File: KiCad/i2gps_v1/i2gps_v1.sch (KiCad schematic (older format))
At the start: 58 parts, among them IC1 ATMEGA8-AI, P1 I/O, P10 CD2, P11 CD2, P12 CD1, P13 CD1, P2 COMM_R, P3 BootDrive, P4 CONN_6, P5 CONN_6, P6 CONN_2, P7 GPS_UP501, P8 FTDI, P9 ISP, SW1 SW_PUSH, U1 MCP1700T-3302E/TT, U2 74HC125, U3 MIC5219-5.0BM5, X1 CRYSTAL_2

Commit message: i2gps_v1 : some minor mods. uploading so I can go home and work on it.
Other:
- note added: "B14 (PD5)\nBootDrive Header"
- note added: "B_03 (PD2)\nGPS 1pps"
- note added: "B_12 (PD7)\nSQW (1pps) signal"
- note removed: "B14 (PD5) : for\nBootDrive Header"
- note removed: "B_03 : GPS 1pps"
- note removed: "SQW signal\ncomes to PD7 / B12"
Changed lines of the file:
@@
-EESchema Schematic File Version 2  date 2/23/2012 11:50:56 AM
+EESchema Schematic File Version 2  date 2/23/2012 5:46:03 PM
 LIBS:i2gps_v1
 LIBS:power
@@
 Comment4 ""
 $EndDescr
-Text Notes 7050 6300 0    60   Italic 12
-GPS Breakout
+Wire Notes Line
+	4050 3925 4050 3775
+Wire Notes Line
+	4050 3925 4750 3925
+Wire Notes Line
+	4750 3925 4750 3775
+Wire Notes Line
+	4750 3775 4050 3775
 Wire Notes Line
 	7050 7025 7050 6300
@@
 Connection ~ 10600 1850
 Wire Notes Line
-	4750 3675 4050 3675
-Wire Notes Line
-	4750 3675 4750 3525
-Wire Notes Line
-	4750 3525 4050 3525
-Wire Notes Line
-	4050 3525 4050 3675
+	4750 3750 4050 3750
+Wire Notes Line
+	4750 3750 4750 3600
+Wire Notes Line
+	4750 3600 4050 3600
+Wire Notes Line
+	4050 3600 4050 3750
 Wire Wire Line
 	4000 6900 3625 6900
@@
 Connection ~ 5000 2650
 Wire Wire Line
-	4800 1700 4800 4775
+	4800 1775 4800 4850
 Connection ~ 4800 2750
 Wire Wire Line
@@
 	10850 6700 10950 6700
 Wire Notes Line
-	4750 3750 4050 3750
-Wire Notes Line
-	4750 3750 4750 3950
-Wire Notes Line
-	4750 3950 4050 3950
-Wire Notes Line
-	4050 3950 4050 3750
-Wire Notes Line
 	3550 6300 4525 6300
 Wire Notes Line
@@
 	7675 6800 7275 6800
 Wire Notes Line
-	4750 3275 4050 3275
-Wire Notes Line
-	4750 3275 4750 3375
-Wire Notes Line
-	4750 3375 4050 3375
-Wire Notes Line
-	4050 3375 4050 3275
-Text Notes 4100 3350 0    40   Italic 8
-B_03 : GPS 1pps
+	4750 3425 4050 3425
+Wire Notes Line
+	4750 3425 4750 3575
+Wire Notes Line
+	4750 3575 4050 3575
+Wire Notes Line
+	4050 3575 4050 3425
+Text Notes 7050 6300 0    60   Italic 12
+GPS Breakout
+Text Notes 4100 3500 0    40   Italic 8
+B_03 (PD2)\nGPS 1pps
 Text Label 7275 6900 0    50   ~ 0
 B_03
@@
 Text Label 3625 6800 0    50   ~ 0
 B_14
-Text Notes 4100 3600 0    40   Italic 8
-B14 (PD5) : for\nBootDrive Header
+Text Notes 4100 3675 0    40   Italic 8
+B14 (PD5)\nBootDrive Header
 Text Label 3625 6900 0    50   ~ 0
 RXD
@@
 3V3
 Text Notes 4075 3850 0    40   Italic 8
-SQW signal\ncomes to PD7 / B12
+B_12 (PD7)\nSQW (1pps) signal
 Text Label 10950 6900 0    60   ~ 0
 BAT

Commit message: i2gps_v1 : this project is merged with i2sd_v3. GPS header to be added
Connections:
- net labels removed: B_12
- wire segments 236 -> 235
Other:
- note added: "B_12 (PD7)\nSQW (1Hz) signal"
- note removed: "B_12 (PD7)\nSQW (1pps) signal"
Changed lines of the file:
@@
-EESchema Schematic File Version 2  date 2/23/2012 5:46:03 PM
+EESchema Schematic File Version 2  date 3/9/2012 6:29:21 PM
 LIBS:i2gps_v1
 LIBS:power
@@
 Sheet 1 2
 Title "Buckler, i2sd, v3, with RTC, with HW addressing"
-Date "23 feb 2012"
+Date "9 mar 2012"
 Rev "3"
 Comp "WyoLum"
@@
 Comment4 ""
 $EndDescr
+Wire Wire Line
+	3400 2750 4800 2750
 Wire Notes Line
 	4050 3925 4050 3775
@@
 Connection ~ 6300 6700
 Wire Wire Line
-	6300 6700 6300 6800
+	6300 6800 6300 6700
 Wire Wire Line
 	6300 6800 6400 6800
@@
 	2900 7000 2000 7000
 Wire Wire Line
-	2700 7300 2700 7200
+	2700 7200 2700 7300
 Connection ~ 10600 2400
 Wire Wire Line
-	10850 2575 10850 2400
+	10850 2400 10850 2575
 Wire Wire Line
 	10850 2575 10700 2575
@@
 	10650 1350 10650 1450
 Wire Wire Line
-	10925 1350 10925 1450
+	10925 1450 10925 1350
 Wire Wire Line
 	10925 1450 8875 1450
@@
 	10400 850  10325 850
 Wire Wire Line
-	10325 1000 10450 1000
+	10450 1000 10325 1000
 Wire Wire Line
 	10450 1000 10450 700
@@
 Connection ~ 5750 1900
 Wire Wire Line
-	5750 1900 6150 1900
+	6150 1900 5750 1900
 Wire Wire Line
 	6150 1900 6150 1950
 Connection ~ 6300 2450
 Wire Wire Line
-	6150 2450 7100 2450
+	7100 2450 6150 2450
 Wire Wire Line
 	6150 2450 6150 2250
@@
 Connection ~ 5750 3100
 Wire Wire Line
-	6150 3100 5750 3100
+	5750 3100 6150 3100
 Connection ~ 6450 4050
 Wire Wire Line
@@
 	5750 1100 5750 4050
 Wire Wire Line
-	5750 4050 7000 4050
+	7000 4050 5750 4050
 Wire Wire Line
 	7000 4050 7000 4650
@@
 	4800 800  4800 1200
 Wire Wire Line
-	3400 2750 4800 2750
-Wire Wire Line
 	3400 2650 5000 2650
 Wire Wire Line
@@
 	5400 1200 5400 1100
 Wire Wire Line
-	5200 1200 5200 1100
+	5200 1100 5200 1200
 Connection ~ 7600 1100
 Connection ~ 1075 4975
@@
 	1500 2650 975  2650
 Wire Wire Line
-	975  2650 975  800
-Wire Wire Line
-	3400 4350 5400 4350
-Wire Wire Line
-	3400 4250 5200 4250
+	975  800  975  2650
+Wire Wire Line
+	5400 4350 3400 4350
+Wire Wire Line
+	5200 4250 3400 4250
 Connection ~ 8400 2400
 Connection ~ 8025 4975
@@
 	8025 4750 8425 4750
 Wire Wire Line
-	7950 4875 5000 4875
+	5000 4875 7950 4875
 Wire Wire Line
 	2350 800  2350 1950
@@
 	9950 2475 9950 2350
 Wire Wire Line
-	5200 4250 5200 1700
-Wire Wire Line
-	5400 4350 5400 1700
-Wire Wire Line
-	5000 4875 5000 1700
+	5200 1700 5200 4250
+Wire Wire Line
+	5400 1700 5400 4350
+Wire Wire Line
+	5000 1700 5000 4875
 Connection ~ 5000 2650
 Wire Wire Line
-	4800 1775 4800 4850
+	4800 1700 4800 4775
 Connection ~ 4800 2750
 Wire Wire Line
@@
 Connection ~ 7100 4975
 Wire Wire Line
-	7100 2450 7100 4975
+	7100 4975 7100 2450
 Connection ~ 7100 3650
 Wire Wire Line
@@
 	1150 6800 800  6800
 Wire Wire Line
-	6150 3450 6150 3650
-Wire Wire Line
-	6150 3650 7100 3650
+	6150 3650 6150 3450
+Wire Wire Line
+	7100 3650 6150 3650
 Connection ~ 6300 3650
 Wire Wire Line
-	6150 2850 6150 3050
-Wire Wire Line
-	6150 3050 7100 3050
+	6150 3050 6150 2850
+Wire Wire Line
+	7100 3050 6150 3050
 Connection ~ 6300 3050
 Wire Wire Line
@@
 	4950 7050 4950 7000
 Wire Wire Line
-	5250 7450 5250 7500
+	5250 7500 5250 7450
 Wire Wire Line
 	5250 7500 4950 7500
@@
 	5200 1100 8625 1100
 Wire Wire Line
-	8625 1100 8625 1850
-Wire Wire Line
-	8625 1850 9400 1850
+	8625 1850 8625 1100
+Wire Wire Line
+	9400 1850 8625 1850
 Wire Wire Line
 	8875 1450 8875 1300
@@
 Connection ~ 8700 800
 Wire Wire Line
-	10600 1650 8700 1650
-Wire Wire Line
-	8700 1650 8700 650
+	8700 1650 10600 1650
+Wire Wire Line
+	8700 650  8700 1650
 Wire Wire Line
 	10450 800  11150 800
@@
 	1400 3150 1500 3150
 Wire Wire Line
-	4375 4050 4500 4050
-Wire Wire Line
-	4500 4050 4500 4600
+	4500 4050 4375 4050
+Wire Wire Line
+	4500 4600 4500 4050
 Wire Notes Line
 	4425 4600 3325 4600
@@
 	7750 1950 7650 1950
 Wire Wire Line
-	7650 1950 7650 2400
-Wire Wire Line
-	7650 2400 10850 2400
+	7650 2400 7650 1950
+Wire Wire Line
+	10850 2400 7650 2400
 Wire Wire Line
 	8500 2400 8500 2250
@@
 	700  2575 700  2550
 Wire Wire Line
-	700  2550 900  2550
-Wire Wire Line
-	900  2550 900  2850
+	900  2550 700  2550
+Wire Wire Line
+	900  2850 900  2550
 Connection ~ 900  2800
 Wire Wire Line
-	550  3050 550  4975
-Wire Wire Line
-	550  4975 8025 4975
+	550  4975 550  3050
+Wire Wire Line
+	8025 4975 550  4975
 Wire Wire Line
 	4000 2100 4000 2550
@@
 Wire Wire Line
 	4100 2250 4100 2100
-Wire Wire Line
-	10850 6100 10950 6100
 Wire Wire Line
 	10850 6700 10950 6700
@@
 BAT
 Text Label 7275 6700 0    50   ~ 0
-5V0
+3V3
 Text Label 7275 6600 0    50   ~ 0
 GND
 Text Label 7275 6500 0    50   ~ 0
+RXD
+Text Label 7275 6400 0    50   ~ 0
 TXD
-Text Label 7275 6400 0    50   ~ 0
-RXD
 $Comp
 L CONN_6 P7
@@
 F8 "32k" I R 10850 6800 60
 F9 "BAT" I R 10850 6900 60
-F10 "B_12" I R 10850 6100 60
 $EndSheet
 $Comp
@@
 3V3
 Text Notes 4075 3850 0    40   Italic 8
-B_12 (PD7)\nSQW (1pps) signal
+B_12 (PD7)\nSQW (1Hz) signal
 Text Label 10950 6900 0    60   ~ 0
 BAT
@@
 Text Label 8325 3850 0    40   ~ 0
 RST
-Text Label 10950 6100 0    50   ~ 0
-B_12
 Text Notes 4250 1700 1    50   ~ 0
 +5V
@@
 B_13
 Text Label 3400 3850 0    60   ~ 0
-B_12
+SQW
 Text Label 3400 4050 0    60   ~ 0
 B_11

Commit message: 
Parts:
- removed P2: COMM_R, PIN_ARRAY_4x1, symbol CONN_4
- C1, C2, C8: footprint CP_5x11mm -> c_0805
- C10, C3, C4, C7: footprint C2 -> c_0805
- C11: footprint cnp_3mm_disc -> c_0805
- C6: footprint C2 -> C_ELCO_SMD
- D1, D2: footprint led_5mm_clear -> d_0805
- P1: footprint pin_strip_8 -> I/O
- P10, P11: footprint vite_4mm -> Sck-04-F-SMT
- P13: footprint pin_strip_3x2 -> Sck-04-F-SMT
- P3: footprint pin_strip_6-90 -> PIN_ARRAY-6X1
- P7: footprint (none) -> PIN_ARRAY-6X1
- P8: footprint vite_4mm -> PIN_ARRAY-6X1
- P9: footprint vite_4mm -> ISP
- R1, R2, R3, R4, R5, R6, R7, R8: footprint rc03_vert_LED -> r_0805
- SW1: footprint SW_PB_V -> SW_SMD
- U1: footprint dil_16-300_socket -> SOT23-3
- U2: footprint TO-220_Horizontal -> SO14E
- U3: footprint dil_28-300_socket -> SOT23-5
- X1: footprint XTAL -> Xtal_SMD2
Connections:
- net labels added: 1pps, ADC6, ADC7, Boot, Ir_Dat, LED1, LED2, PB0, PB1, PB6, PB7, PC0, PC1, PC2, PD6
- net labels removed: B_01, B_02, B_03, B_04, B_05, B_06, B_07, B_08, B_09, B_10, B_11, B_13, B_14
- wire segments 235 -> 226
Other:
- note added: "BUCKLER Interface"
- note added: "Mounting Hole"
- note added: "PD2 (1pps)\nGPS 1pps signal"
- note added: "PD5 (Boot)\nBootDrive Header"
- note added: "PD7 (SQW)\nRTC 1Hz signal"
- note removed: "(PD5)"
- note removed: "B14 (PD5)\nBootDrive Header"
- note removed: "B_03 (PD2)\nGPS 1pps"
- note removed: "B_12 (PD7)\nSQW (1Hz) signal"
- note removed: "I/O BREAKOUT"
- note removed: "Mounting\nHole"
- note removed: "P3 : COMM_L removed\nto reduce board size"
- note removed: "VCC\nSCL\nSDA\nGND"
- moved on the sheet: P10, P11, P12, P13, PCB1, SC1

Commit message: I2GPS_v1 : SQW/LED2 swapped, GPS Tx/Rx pins changed, Gerber plots generated
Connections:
- net labels added: GPS_Rx, GPS_Tx
- net labels removed: ADC7, PD6
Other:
- moved on the sheet: B12
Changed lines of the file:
@@
-EESchema Schematic File Version 2  date 3/10/2012 5:22:51 PM
+EESchema Schematic File Version 2  date 3/12/2012 5:57:10 PM
 LIBS:i2gps_v1
 LIBS:power
@@
 Sheet 1 2
 Title "Buckler, i2sd, v3, with RTC, with HW addressing"
-Date "10 mar 2012"
+Date "12 mar 2012"
 Rev "3"
 Comp "WyoLum"
@@
 Comment4 ""
 $EndDescr
+Text Label 7275 6400 0    50   ~ 0
+GPS_Rx
 Text Label 1400 3275 0    50   ~ 0
 PB7
@@
 GND
 Text Label 7275 6500 0    50   ~ 0
-RXD
-Text Label 7275 6400 0    50   ~ 0
-TXD
+GPS_Tx
 $Comp
 L CONN_6 P7
@@
 L I/O B12
 U 1 1 4DCD1D52
-P 3775 3850
-F 0 "B12" H 3855 3850 40  0000 L CNN
-F 1 "I/O" H 3775 3905 30  0001 C CNN
-F 2 "I/O" H 3775 3850 60  0001 C CNN
-	1    3775 3850
+P 3775 3450
+F 0 "B12" H 3855 3450 40  0000 L CNN
+F 1 "I/O" H 3775 3505 30  0001 C CNN
+F 2 "I/O" H 3775 3450 60  0001 C CNN
+	1    3775 3450
 	1    0    0    -1
 $EndComp
@@
 Boot
 Text Label 3400 3750 0    60   ~ 0
-PD6
-Text Label 3400 3850 0    60   ~ 0
+GPS_Tx
+Text Label 3400 3450 0    60   ~ 0
 SQW
 Text Label 3400 4050 0    60   ~ 0
@@
 PB1
 Text Label 3400 2950 0    60   ~ 0
-ADC7
+GPS_Rx
 Text Label 3400 2250 0    60   ~ 0
 PC0
@@
 Text Label 3625 3350 0    60   ~ 0
 1pps
-Text Label 3625 3450 0    60   ~ 0
+Text Label 3625 3850 0    60   ~ 0
 LED2
 Text Label 3400 3550 0    60   ~ 0

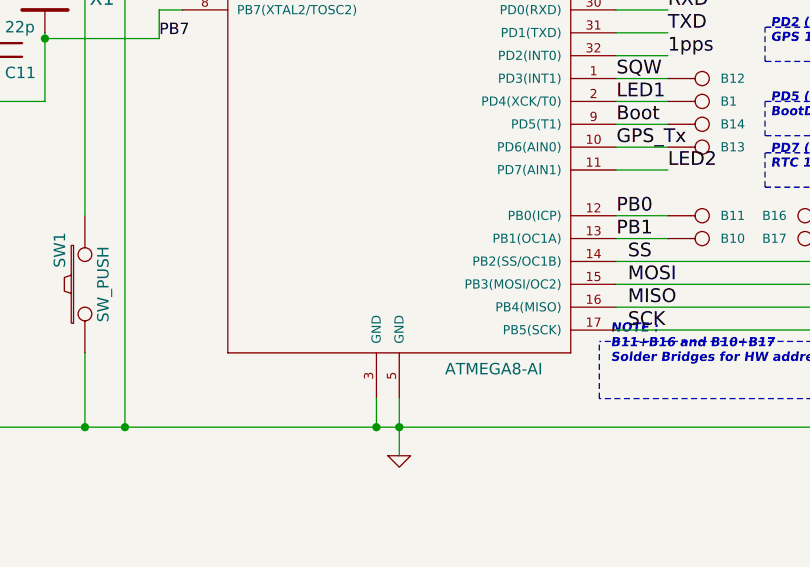
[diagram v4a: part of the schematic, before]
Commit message: i2gps final BoM, Gerbers (changed ATMega8 to ATMega328)
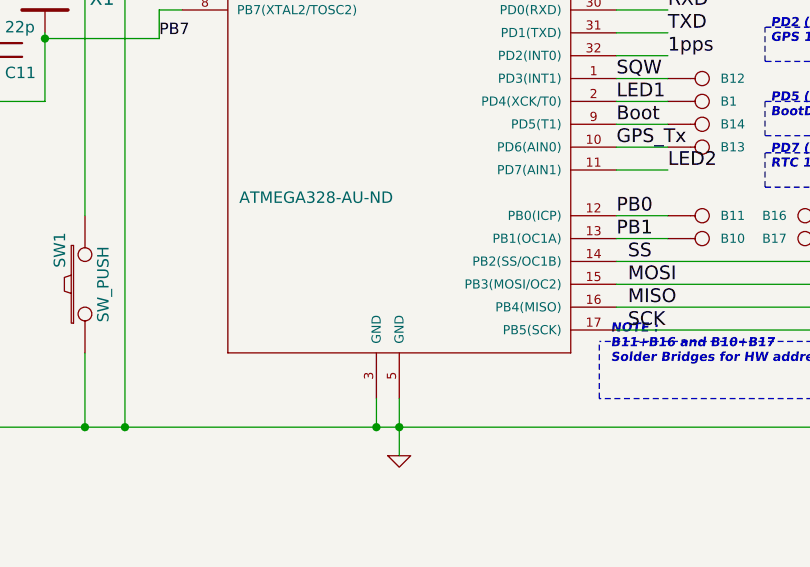
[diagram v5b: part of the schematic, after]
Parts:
- IC1: value ATMEGA8-AI -> ATMEGA328-AU-ND
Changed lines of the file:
@@
-EESchema Schematic File Version 2  date 3/12/2012 5:57:10 PM
+EESchema Schematic File Version 2  date Sunday 15 April 2012 01:54:18 AM IST
 LIBS:i2gps_v1
 LIBS:power
@@
 Sheet 1 2
 Title "Buckler, i2sd, v3, with RTC, with HW addressing"
-Date "12 mar 2012"
+Date "14 apr 2012"
 Rev "3"
 Comp "WyoLum"
@@
 P 2400 3250
 F 0 "IC1" H 1700 4400 50  0000 L BNN
-F 1 "ATMEGA8-AI" H 2650 1750 50  0000 L BNN
+F 1 "ATMEGA328-AU-ND" H 1750 2500 50  0000 L BNN
 F 2 "TQFP32" H 2925 1675 50  0001 C CNN
 	1    2400 3250

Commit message: i2gps : FINAL Production Files. Protection diodes added for GPS. Minor mods to schematic, pcb silk screen etc.
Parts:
- added D3, D4: RB886GT2R, d_VMD2, symbol DIODESCH
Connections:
- net labels added: GPS_3V3, GPS_BAT
- wire segments 226 -> 229
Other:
- note added: "BUCKLER Header"
- note added: "GPS Header"
- note removed: "BUCKLER Interface"
- note removed: "GPS Breakout"
- moved on the sheet: P7

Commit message: i2gps : error in Silk screen rectified.
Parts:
- P6: value CONN_2 -> 9VBAT
- R5, R8: value 470E -> 1k5
- U1: value MCP1700T-3302E/TT -> 3V3; Part No (none) -> MCP1700T-3302E/TT
- U3: value MIC5219-5.0BM5 -> 5V0; Part No (none) -> MIC5219-5.0BM5
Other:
- note added: "MCP1700T-3302E/TT"
- note added: "MIC5219-5.0BM5"
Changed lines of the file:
@@
-EESchema Schematic File Version 2  date 4/27/2012 5:56:55 PM
+EESchema Schematic File Version 2  date 4/28/2012 11:01:58 AM
 LIBS:i2gps_v1
 LIBS:power
@@
 Sheet 1 2
 Title "Buckler+i2sd+RTC+HW addr+GPS+uSD+IRrx"
-Date "27 apr 2012"
+Date "28 apr 2012"
 Rev "1"
 Comp "WyoLum"
@@
 Comment4 ""
 $EndDescr
+Text Notes 9450 600  0    50   ~ 0
+MIC5219-5.0BM5
+Text Notes 9400 1750 0    50   ~ 0
+MCP1700T-3302E/TT
 Wire Notes Line
 	8850 6300 7025 6300
@@
 PB6
 $Comp
-L GND #PWR7
+L GND #PWR01
 U 1 1 4F5AFC62
 P 2450 5100
-F 0 "#PWR7" H 2450 5100 30  0001 C CNN
+F 0 "#PWR01" H 2450 5100 30  0001 C CNN
 F 1 "GND" H 2450 5030 30  0001 C CNN
 	1    2450 5100
@@
 IR SENSOR
 $Comp
-L GND #PWR4
+L GND #PWR02
 U 1 1 4EC6563E
 P 4100 2250
-F 0 "#PWR4" H 4100 2250 30  0001 C CNN
+F 0 "#PWR02" H 4100 2250 30  0001 C CNN
 F 1 "GND" H 4100 2180 30  0001 C CNN
 	1    4100 2250
@@
 GND
 $Comp
-L GND #PWR6
+L GND #PWR03
 U 1 1 4E96D558
 P 4500 4600
-F 0 "#PWR6" H 4500 4600 30  0001 C CNN
+F 0 "#PWR03" H 4500 4600 30  0001 C CNN
 F 1 "GND" H 4500 4530 30  0001 C CNN
 	1    4500 4600
@@
 GND
 $Comp
-L +3.3V #PWR2
+L +3.3V #PWR04
 U 1 1 4E1EF3E1
 P 7600 975
-F 0 "#PWR2" H 7600 935 30  0001 C CNN
+F 0 "#PWR04" H 7600 935 30  0001 C CNN
 F 1 "+3.3V" H 7600 1085 30  0000 C CNN
 	1    7600 975
@@
 P 10350 2675
 F 0 "P6" V 10300 2675 40  0000 C CNN
-F 1 "CONN_2" V 10400 2675 40  0000 C CNN
+F 1 "9VBAT" V 10400 2675 40  0000 C CNN
 F 2 "pin_strip_2" H 10350 2675 60  0001 C CNN
 	1    10350 2675
@@
 U 1 1 4E1ECD8D
 P 9875 850
-F 0 "U3" H 9875 650 60  0000 C CNN
-F 1 "MIC5219-5.0BM5" H 9875 1150 60  0000 C CNN
+F 0 "U3" H 9700 550 60  0000 C CNN
+F 1 "5V0" H 10050 550 60  0000 C CNN
 F 2 "SOT23-5" H 9875 850 60  0001 C CNN
+F 4 "MIC5219-5.0BM5" H 9875 850 60  0001 C CNN "Part No"
 	1    9875 850
 	-1   0    0    -1
 $EndComp
 $Comp
-L GND #PWR3
+L GND #PWR05
 U 1 1 4E1EC9C3
 P 9950 1525
-F 0 "#PWR3" H 9950 1525 30  0001 C CNN
+F 0 "#PWR05" H 9950 1525 30  0001 C CNN
 F 1 "GND" H 9950 1455 30  0001 C CNN
 	1    9950 1525
@@
 LED2
 $Comp
-L GND #PWR8
+L GND #PWR06
 U 1 1 4DCFFB44
 P 5100 7550
-F 0 "#PWR8" H 5100 7550 30  0001 C CNN
+F 0 "#PWR06" H 5100 7550 30  0001 C CNN
 F 1 "GND" H 5100 7480 30  0001 C CNN
 	1    5100 7550
@@
 P 5250 6750
 F 0 "R8" V 5330 6750 50  0000 C CNN
-F 1 "470E" V 5250 6750 50  0000 C CNN
+F 1 "1k5" V 5250 6750 50  0000 C CNN
 F 2 "r_0805" H 5250 6750 60  0001 C CNN
 	1    5250 6750
@@
 P 4950 6750
 F 0 "R5" V 5030 6750 50  0000 C CNN
-F 1 "470E" V 4950 6750 50  0000 C CNN
+F 1 "1k5" V 4950 6750 50  0000 C CNN
 F 2 "r_0805" H 4950 6750 60  0001 C CNN
 	1    4950 6750
@@
 GND
 $Comp
-L GND #PWR5
+L GND #PWR07
 U 1 1 4DCAC327
 P 9950 2475
-F 0 "#PWR5" H 9950 2475 30  0001 C CNN
+F 0 "#PWR07" H 9950 2475 30  0001 C CNN
 F 1 "GND" H 9950 2405 30  0001 C CNN
 	1    9950 2475
@@
 U 1 1 4DCAC2D1
 P 9950 1950
-F 0 "U1" H 9750 1800 60  0000 C CNN
-F 1 "MCP1700T-3302E/TT" H 9950 2200 60  0000 C CNN
+F 0 "U1" H 9800 1800 60  0000 C CNN
+F 1 "3V3" H 10100 1800 60  0000 C CNN
 F 2 "SOT23-3" H 9950 1950 60  0001 C CNN
+F 4 "MCP1700T-3302E/TT" H 9950 1950 60  0001 C CNN "Part No"
 	1    9950 1950
 	-1   0    0    -1
@@
 $EndComp
 $Comp
-L +5V #PWR1
+L +5V #PWR08
 U 1 1 4D82B1D1
 P 8700 650
-F 0 "#PWR1" H 8700 740 20  0001 C CNN
+F 0 "#PWR08" H 8700 740 20  0001 C CNN
 F 1 "+5V" H 8700 740 30  0000 C CNN
 	1    8700 650

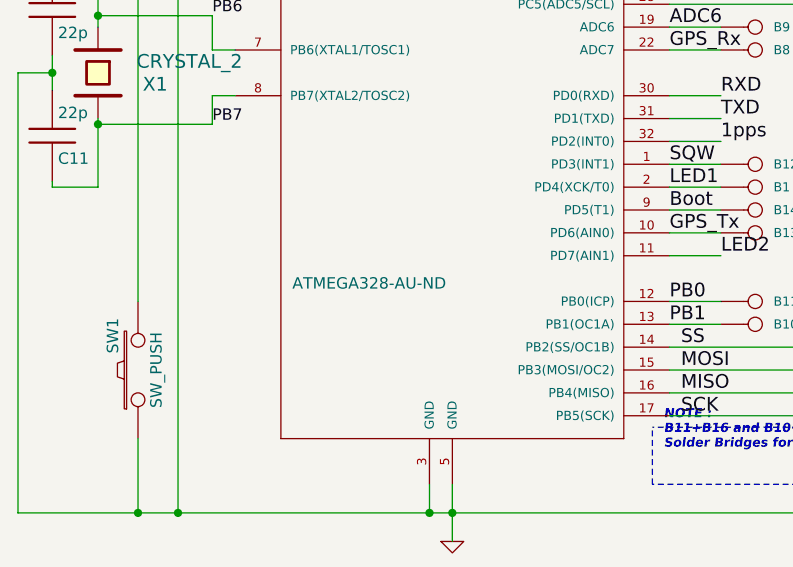
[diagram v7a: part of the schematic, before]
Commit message: i2gps : replaced ATMega328 with ATMega328P , BoM sheet
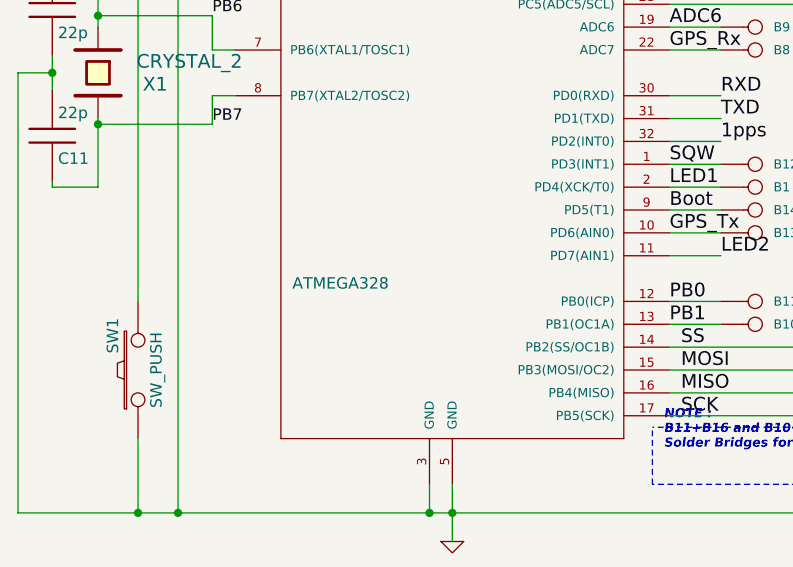
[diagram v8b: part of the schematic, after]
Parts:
- IC1: value ATMEGA328-AU-ND -> ATMEGA328
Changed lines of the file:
@@
-EESchema Schematic File Version 2  date 4/28/2012 11:01:58 AM
+EESchema Schematic File Version 2  date 5/2/2012 7:03:54 PM
 LIBS:i2gps_v1
 LIBS:power
@@
 Sheet 1 2
 Title "Buckler+i2sd+RTC+HW addr+GPS+uSD+IRrx"
-Date "28 apr 2012"
+Date "2 may 2012"
 Rev "1"
 Comp "WyoLum"
@@
 P 2400 3250
 F 0 "IC1" H 1700 4400 50  0000 L BNN
-F 1 "ATMEGA328-AU-ND" H 1750 2500 50  0000 L BNN
+F 1 "ATMEGA328" H 1750 2500 50  0000 L BNN
 F 2 "TQFP32" H 2925 1675 50  0001 C CNN
 	1    2400 3250
